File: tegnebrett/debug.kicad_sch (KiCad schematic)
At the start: 28 parts, among them J6 FPGA_Header_Pin, J9 FPGA_debug1, SW6 FPGA_Button, U1 XC7A100T-2FTG256I, U2 Oscillator 100MHz, U8 IS66WVH16M8DBLL-100B1LI1

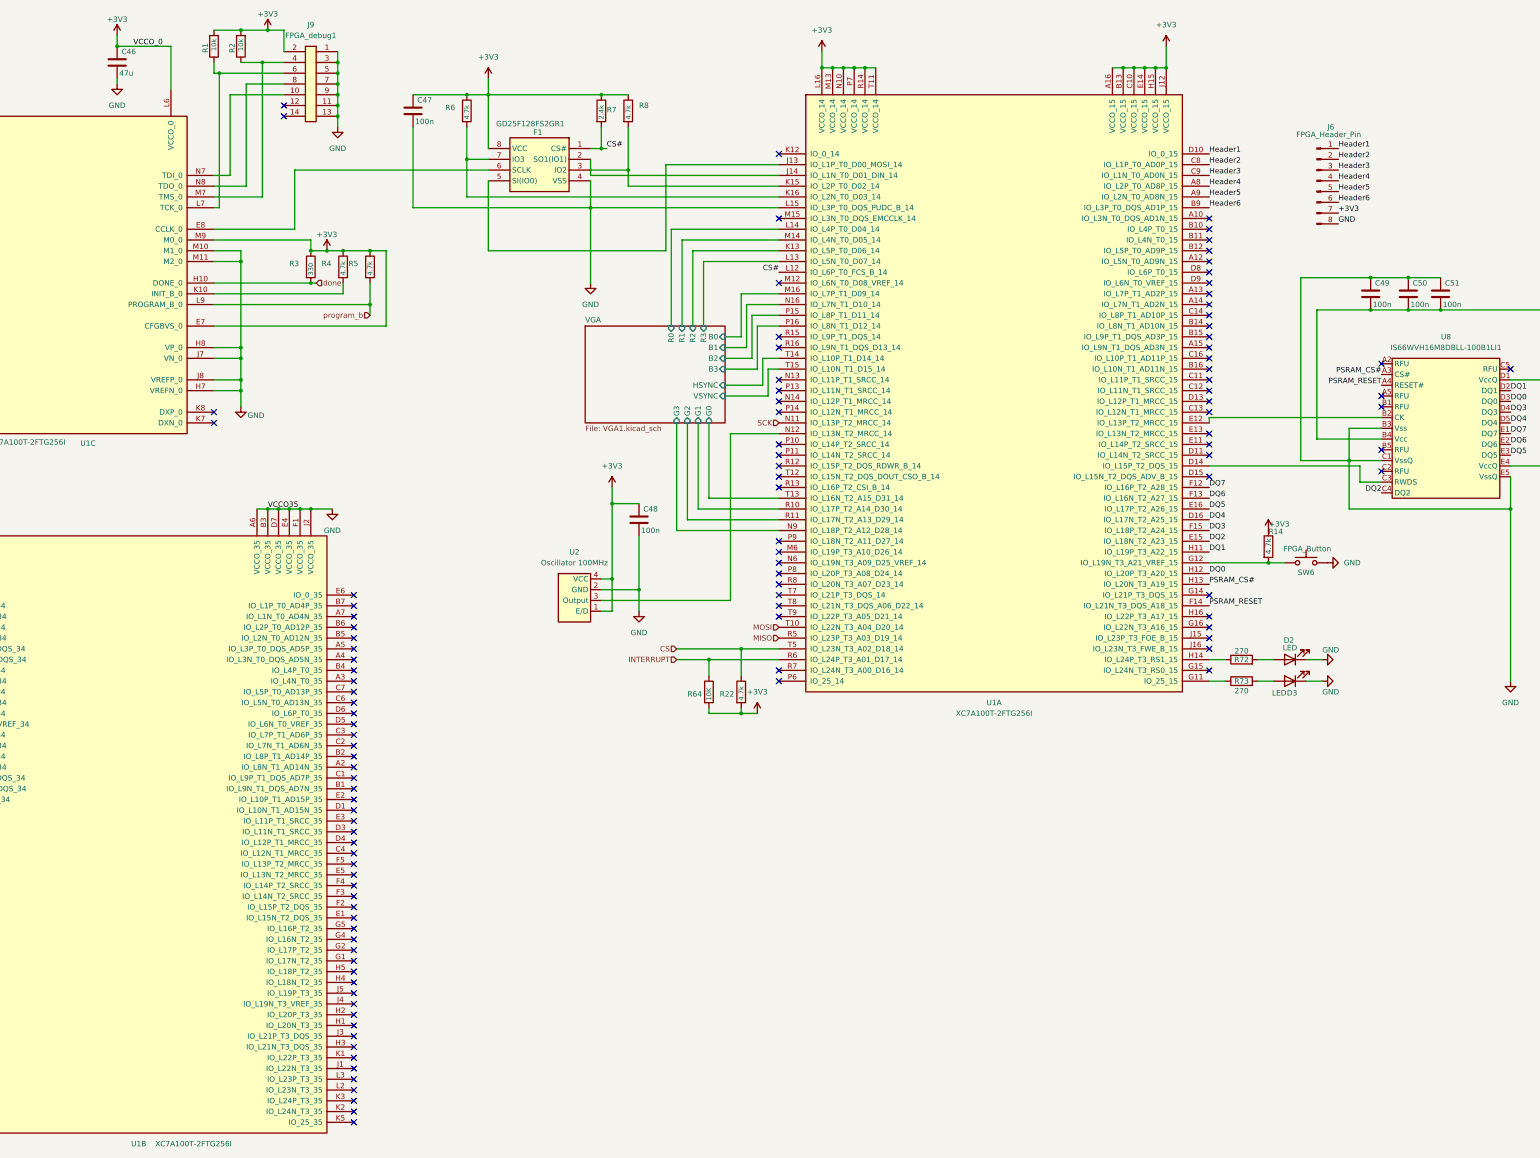
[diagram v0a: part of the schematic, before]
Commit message: refactor: re-annotate schematic labels
References for schematic capacitors (for example C74 -> C2), etc.
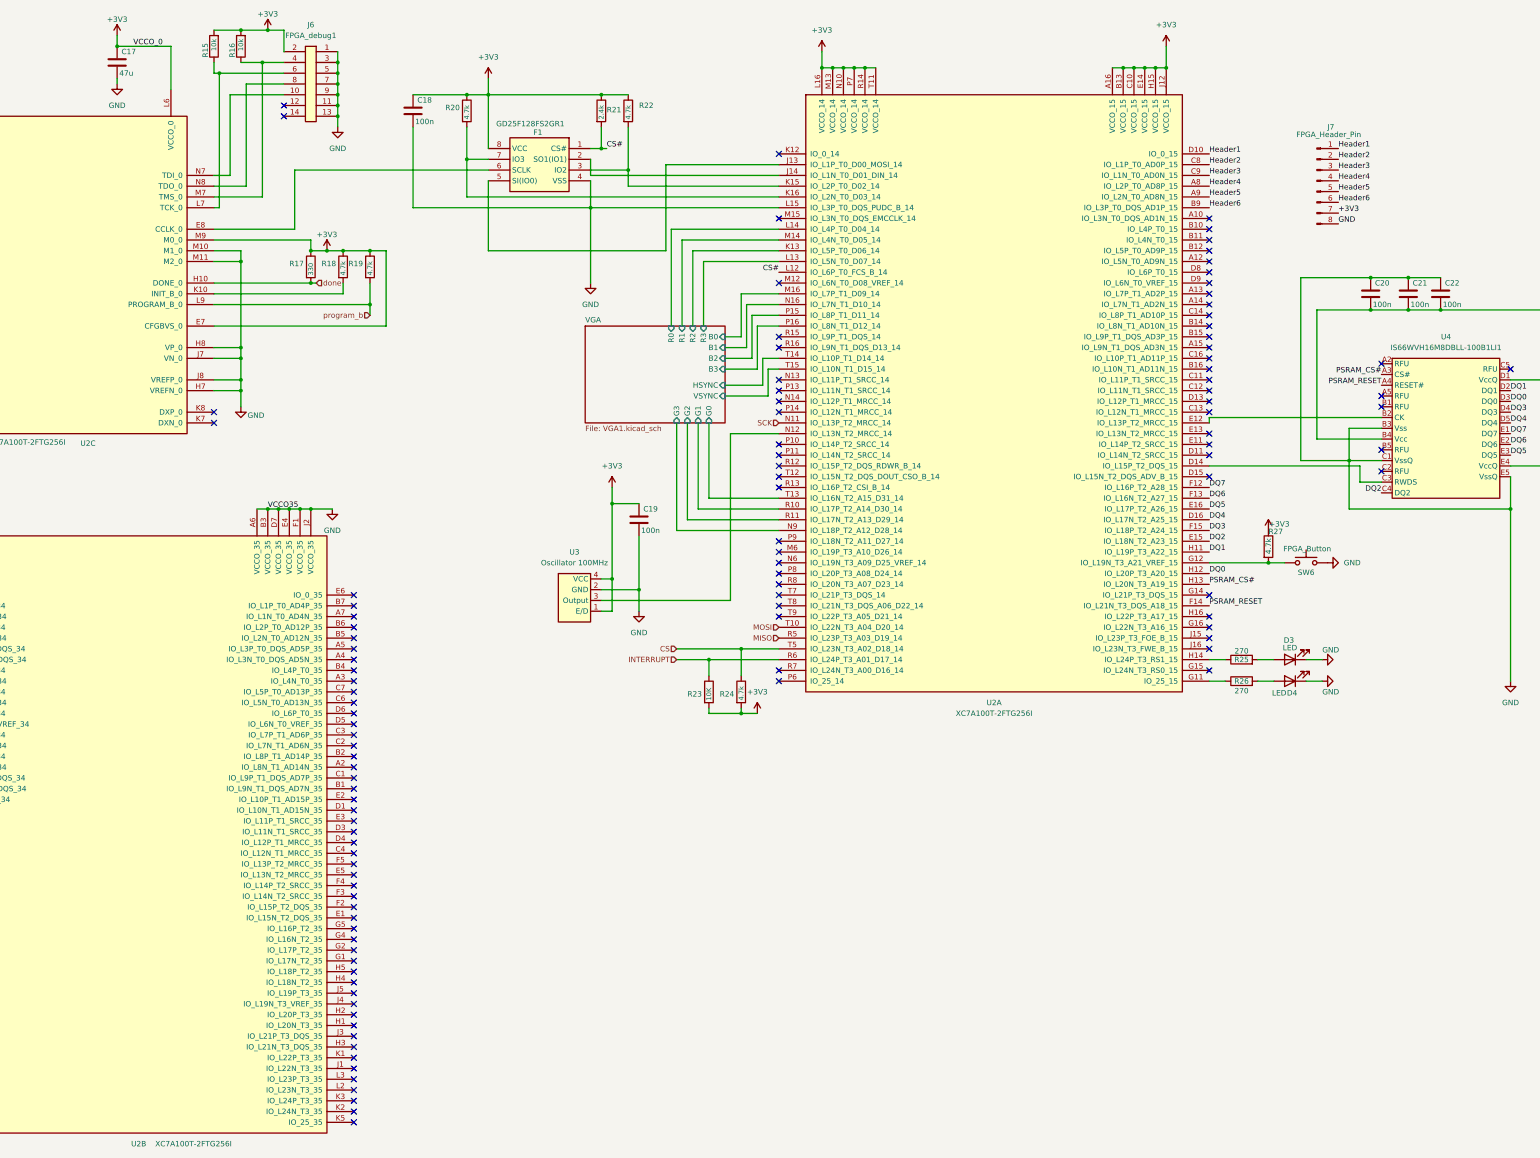
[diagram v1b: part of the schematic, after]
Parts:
- renumbered C46 to C17, C47 to C18, C48 to C19, C49 to C20, C50 to C21, C51 to C22, D2 to D3, D3 to D4, J9 to J6, J6 to J7, R1 to R15, R2 to R16, R3 to R17, R4 to R18, R5 to R19, R6 to R20, R7 to R21, R8 to R22, R64 to R23, R22 to R24, R72 to R25, R73 to R26, R14 to R27, U1 to U2, U2 to U3, U8 to U4

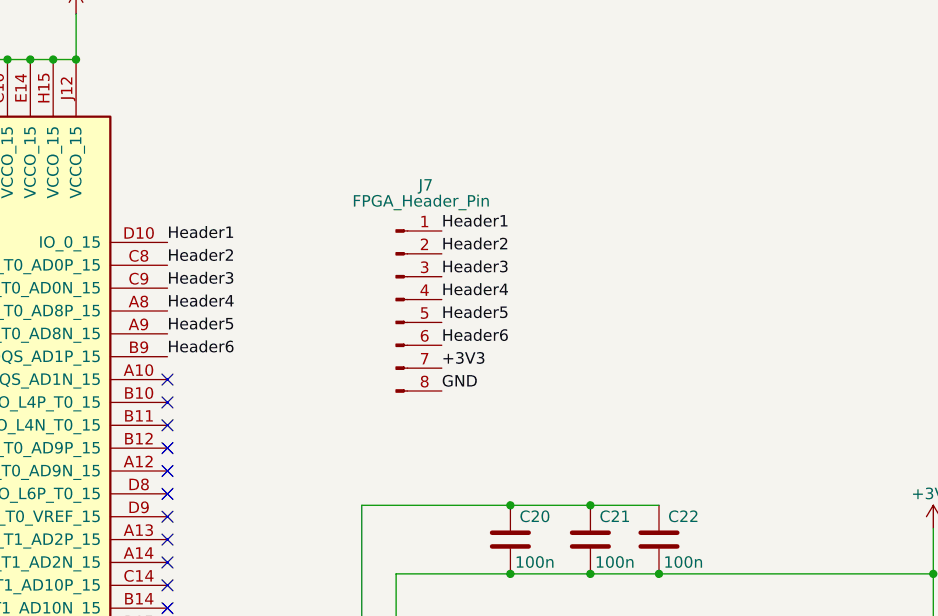
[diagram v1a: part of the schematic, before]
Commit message: refactor: make FPGA_Header_Pin 2x7 instead of 1x8
We'll get some more GPIO pins exposed.
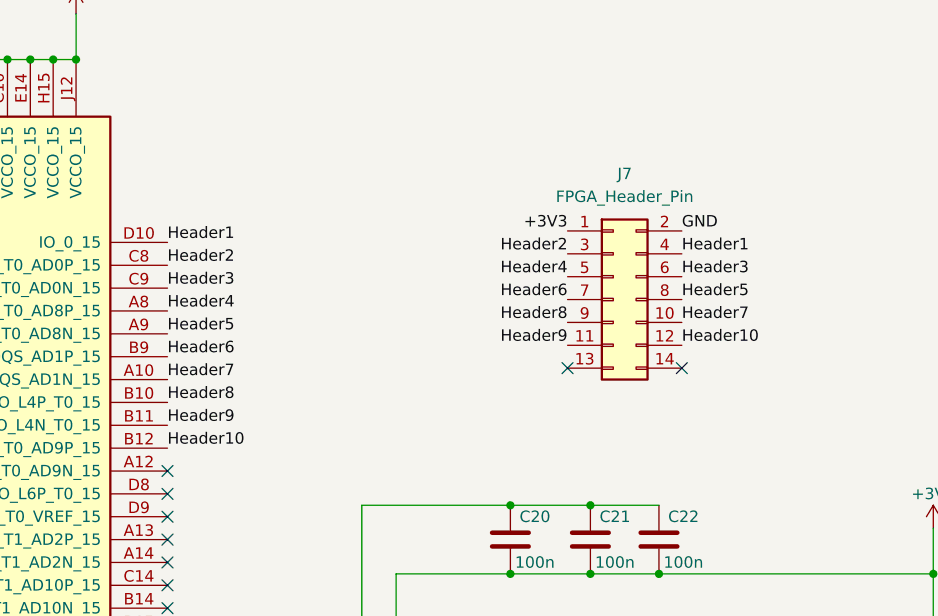
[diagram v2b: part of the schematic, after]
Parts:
- removed J7: FPGA_Header_Pin, Connector_PinHeader_2.54mm:PinHeader_1x08_P2.54mm_Vertical, symbol Connector:Conn_01x08_Pin
- added J7: FPGA_Header_Pin, Connector_PinHeader_2.54mm:PinHeader_2x07_P2.54mm_Vertical, symbol Connector_Generic:Conn_02x07_Odd_Even
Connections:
- net +3V3: now also J7.1 (Pin_1)
- net GND: now also J7.2 (Pin_2)
- net Header1: now also J7.4 (Pin_4)
- net Header2: now also J7.3 (Pin_3)
- net Header3: now also J7.6 (Pin_6)
- net Header4: now also J7.5 (Pin_5)
- net Header5: now also J7.8 (Pin_8)
- net Header6: now also J7.7 (Pin_7)
- net Header7: now reaches U2.A10 (IO_L3N_T0_DQS_AD1N_15)
- net Header7: now also J7.10 (Pin_10)
- net Header8: now reaches U2.B10 (IO_L4P_T0_15)
- net Header8: now also J7.9 (Pin_9)
- net Header9: now reaches U2.B11 (IO_L4N_T0_15)
- net Header9: now also J7.11 (Pin_11)
- net Header10: now reaches U2.B12 (IO_L5P_T0_AD9P_15)
- net Header10: now also J7.12 (Pin_12)
- no-connect marks 133 -> 131
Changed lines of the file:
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@@
 	)
 	(no_connect
+		(at 364.49 62.23)
+	)
+	(no_connect
 		(at 16.51 193.04)
 	)
@@
 	)
 	(no_connect
-		(at 320.04 63.5)
-	)
-	(no_connect
 		(at 118.11 177.8)
 	)
@@
 	)
 	(no_connect
-		(at 320.04 68.58)
-	)
-	(no_connect
 		(at 16.51 200.66)
 	)
@@
 	)
 	(no_connect
-		(at 320.04 71.12)
-	)
-	(no_connect
 		(at 320.04 101.6)
 	)
@@
 	)
 	(no_connect
+		(at 377.19 62.23)
+	)
+	(no_connect
 		(at 320.04 99.06)
 	)
@@
 	)
 	(no_connect
-		(at 320.04 66.04)
-	)
-	(no_connect
 		(at 118.11 185.42)
 	)
@@
 		)
 	)
+	(label "Header9"
+		(at 364.49 59.69 180)
+		(effects
+			(font
+				(size 1.27 1.27)
+			)
+			(justify right bottom)
+		)
+	)
 	(label "Header6"
 		(at 320.04 60.96 0)
@@
 		)
 	)
-	(label "Header5"
-		(at 350.52 57.15 0)
+	(label "Header8"
+		(at 320.04 66.04 0)
 		(effects
 			(font
@@
 		)
 	)
-	(label "Header4"
-		(at 350.52 54.61 0)
+	(label "Header1"
+		(at 377.19 49.53 0)
 		(effects
 			(font
@@
 		)
 	)
-	(label "+3V3"
-		(at 350.52 62.23 0)
+	(label "DQ5"
+		(at 391.16 119.38 0)
 		(effects
 			(font
@@
 		)
 	)
-	(label "Header1"
-		(at 350.52 46.99 0)
+	(label "Header6"
+		(at 364.49 54.61 180)
 		(effects
 			(font
 				(size 1.27 1.27)
 			)
-			(justify left bottom)
+			(justify right bottom)
 		)
 	)
-	(label "DQ5"
-		(at 391.16 119.38 0)
+	(label "PSRAM_CS#"
+		(at 360.68 100.33 180)
 		(effects
 			(font
 				(size 1.27 1.27)
 			)
-			(justify left bottom)
+			(justify right bottom)
 		)
 	)
-	(label "PSRAM_CS#"
-		(at 360.68 100.33 180)
+	(label "Header8"
+		(at 364.49 57.15 180)
 		(effects
 			(font
@@
 		)
 	)
-	(label "Header2"
-		(at 350.52 49.53 0)
+	(label "DQ5"
+		(at 320.04 132.08 0)
 		(effects
 			(font
@@
 		)
 	)
-	(label "DQ5"
-		(at 320.04 132.08 0)
+	(label "Header3"
+		(at 377.19 52.07 0)
 		(effects
 			(font
@@
 		)
 	)
+	(label "Header10"
+		(at 377.19 59.69 0)
+		(effects
+			(font
+				(size 1.27 1.27)
+			)
+			(justify left bottom)
+		)
+	)
+	(label "Header4"
+		(at 364.49 52.07 180)
+		(effects
+			(font
+				(size 1.27 1.27)
+			)
+			(justify right bottom)
+		)
+	)
+	(label "Header5"
+		(at 377.19 54.61 0)
+		(effects
+			(font
+				(size 1.27 1.27)
+			)
+			(justify left bottom)
+		)
+	)
+	(label "+3V3"
+		(at 364.49 46.99 180)
+		(effects
+			(font
+				(size 1.27 1.27)
+			)
+			(justify right bottom)
+		)
+	)
 	(label "DQ4"
 		(at 320.04 134.62 0)
@@
 		)
 	)
-	(label "DQ1"
-		(at 320.04 142.24 0)
+	(label "GND"
+		(at 377.19 46.99 0)
 		(effects
 			(font
@@
 		)
 	)
-	(label "Header3"
-		(at 350.52 52.07 0)
+	(label "DQ1"
+		(at 320.04 142.24 0)
 		(effects
 			(font
@@
 		)
 	)
+	(label "Header10"
+		(at 320.04 71.12 0)
+		(effects
+			(font
+				(size 1.27 1.27)
+			)
+			(justify left bottom)
+		)
+	)
 	(label "DQ7"
 		(at 320.04 127 0)
@@
 		)
 	)
-	(label "GND"
-		(at 350.52 64.77 0)
+	(label "Header7"
+		(at 320.04 63.5 0)
 		(effects
 			(font
@@
 		)
 	)
-	(label "Header6"
-		(at 350.52 59.69 0)
+	(label "Header7"
+		(at 377.19 57.15 0)
 		(effects
 			(font
@@
 		)
 	)
+	(label "Header2"
+		(at 364.49 49.53 180)
+		(effects
+			(font
+				(size 1.27 1.27)
+			)
+			(justify right bottom)
+		)
+	)
 	(label "PSRAM_CS#"
 		(at 320.04 149.86 0)
@@
 		)
 	)
+	(label "Header9"
+		(at 320.04 68.58 0)
+		(effects
+			(font
+				(size 1.27 1.27)
+			)
+			(justify left bottom)
+		)
+	)
 	(label "DQ0"
 		(at 391.16 106.68 0)
@@
 	)
 	(symbol
+		(lib_id "Connector_Generic:Conn_02x07_Odd_Even")
+		(at 369.57 54.61 0)
+		(unit 1)
+		(exclude_from_sim no)
+		(in_bom yes)
+		(on_board yes)
+		(dnp no)
+		(fields_autoplaced yes)
+		(property "Reference" "J7"
+			(at 370.84 40.64 0)
+			(effects
+				(font
+					(size 1.27 1.27)
+				)
+			)
+		)
+		(property "Value" "FPGA_Header_Pin"
+			(at 370.84 43.18 0)
+			(effects
+				(font
+					(size 1.27 1.27)
+				)
+			)
+		)
+		(property "Footprint" "Connector_PinHeader_2.54mm:PinHeader_2x07_P2.54mm_Vertical"
+			(at 369.57 54.61 0)
+			(effects
+				(font
+					(size 1.27 1.27)
+				)
+				(hide yes)
+			)
+		)
+		(property "Datasheet" "~"
+			(at 369.57 54.61 0)
+			(effects
+				(font
+					(size 1.27 1.27)
+				)
+				(hide yes)
+			)
+		)
+		(property "Description" "Generic connector, double row, 02x07, odd/even pin numbering scheme (row 1 odd numbers, row 2 even numbers), script generated (kicad-library-utils/schlib/autogen/connector/)"
+			(at 369.57 54.61 0)
+			(effects
+				(font
+					(size 1.27 1.27)
+				)
+				(hide yes)
+			)
+		)
+		(pin "1"
+		)
+		(pin "6"
+		)
+		(pin "10"
+		)
+		(pin "2"
+		)
+		(pin "4"
+		)
+		(pin "8"
+		)
+		(pin "12"
+		)
+		(pin "14"
+		)
+		(pin "13"
+		)
+		(pin "7"
+		)
+		(pin "5"
+		)
+		(pin "3"
+		)
+		(pin "11"
+		)
+		(pin "9"
+		)
+		(instances
+			(project ""
+				(path "/d9a31669-c5f1-42a7-9461-3df04b9a4e62/5e0df967-c6b5-4cdf-8fe6-93251df44e99"
+					(reference "J7")
+					(unit 1)
+				)
+			)
+		)
+	)
+	(symbol
 		(lib_id "power:GND")
 		(at 113.03 132.08 0)
@@
 					(unit 1)
 				)
-			)
-		)
-	)
-	(symbol
-		(lib_id "Connector:Conn_01x08_Pin")
-		(at 345.44 54.61 0)
-		(unit 1)
-		(exclude_from_sim no)
-		(in_bom yes)
-		(on_board yes)
-		(dnp no)
-		(property "Reference" "J7"
-			(at 348.742 41.91 0)
-			(effects
-				(font
-					(size 1.27 1.27)
-				)
-			)
-		)
-		(property "Value" "FPGA_Header_Pin"
-			(at 348.234 43.688 0)
-			(effects
-				(font
-					(size 1.27 1.27)
-				)
-			)
-		)
-		(property "Footprint" "Connector_PinHeader_2.54mm:PinHeader_1x08_P2.54mm_Vertical"
-			(at 345.44 54.61 0)
-			(effects
-				(font
-					(size 1.27 1.27)
-				)
-				(hide yes)
-			)
-		)
-		(property "Datasheet" "~"
-			(at 345.44 54.61 0)
-			(effects
-				(font
-					(size 1.27 1.27)
-				)
-				(hide yes)
-			)
-		)
-		(property "Description" "Generic connector, single row, 01x08, script generated"
-			(at 345.44 54.61 0)
-			(effects
-				(font
-					(size 1.27 1.27)
-				)
-				(hide yes)
-			)
-		)
-		(pin "5"
-		)
-		(pin "1"
-		)
-		(pin "7"
-		)
-		(pin "6"
-		)
-		(pin "8"
-		)
-		(pin "2"
-		)
-		(pin "3"
-		)
-		(pin "4"
-		)
-		(instances
-			(project ""
-				(path "/d9a31669-c5f1-42a7-9461-3df04b9a4e62/5e0df967-c6b5-4cdf-8fe6-93251df44e99"
-					(reference "J7")
-					(unit 1)
-				)
